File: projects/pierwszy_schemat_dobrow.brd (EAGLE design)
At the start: 100 x 80 mm, 37 parts, among them IC1 74HC595N, IC2 7805T, IC3 LD117AV, J1 DCJ0202

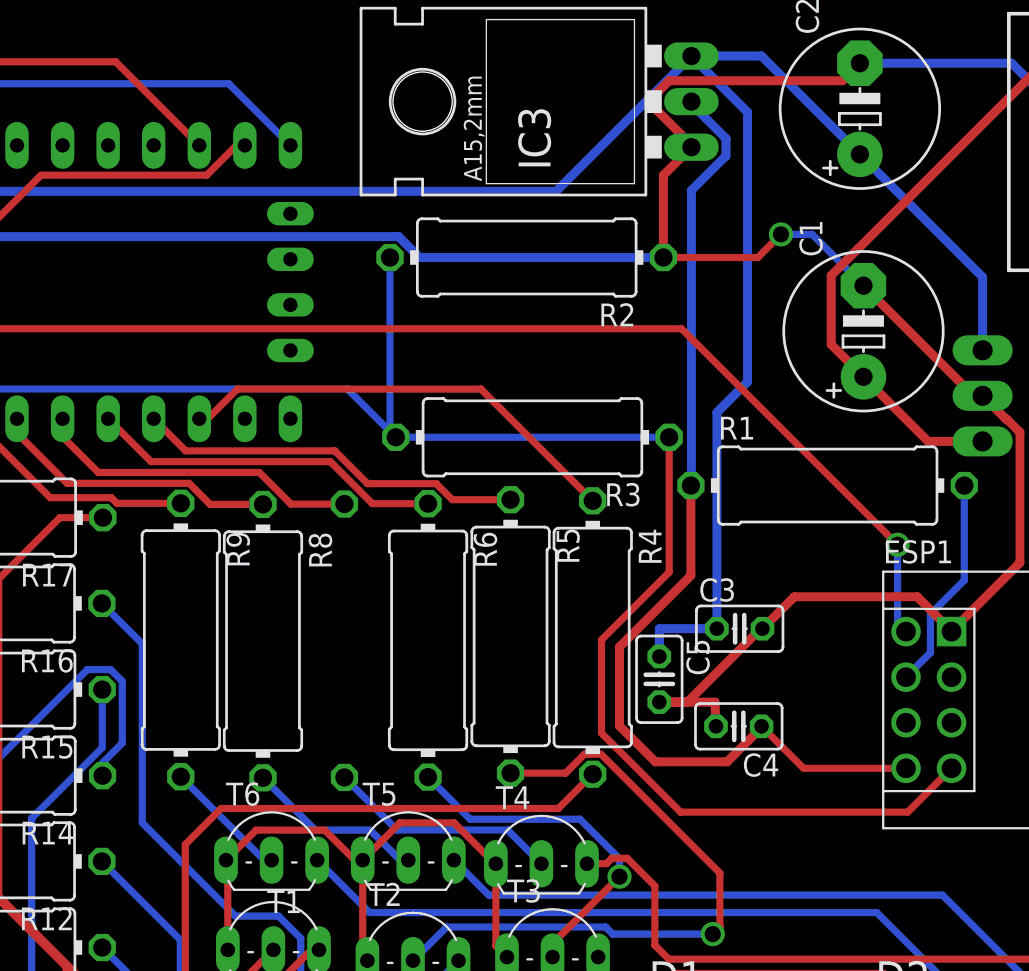
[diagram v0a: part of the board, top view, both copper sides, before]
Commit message: moved resistors for better thermal flow
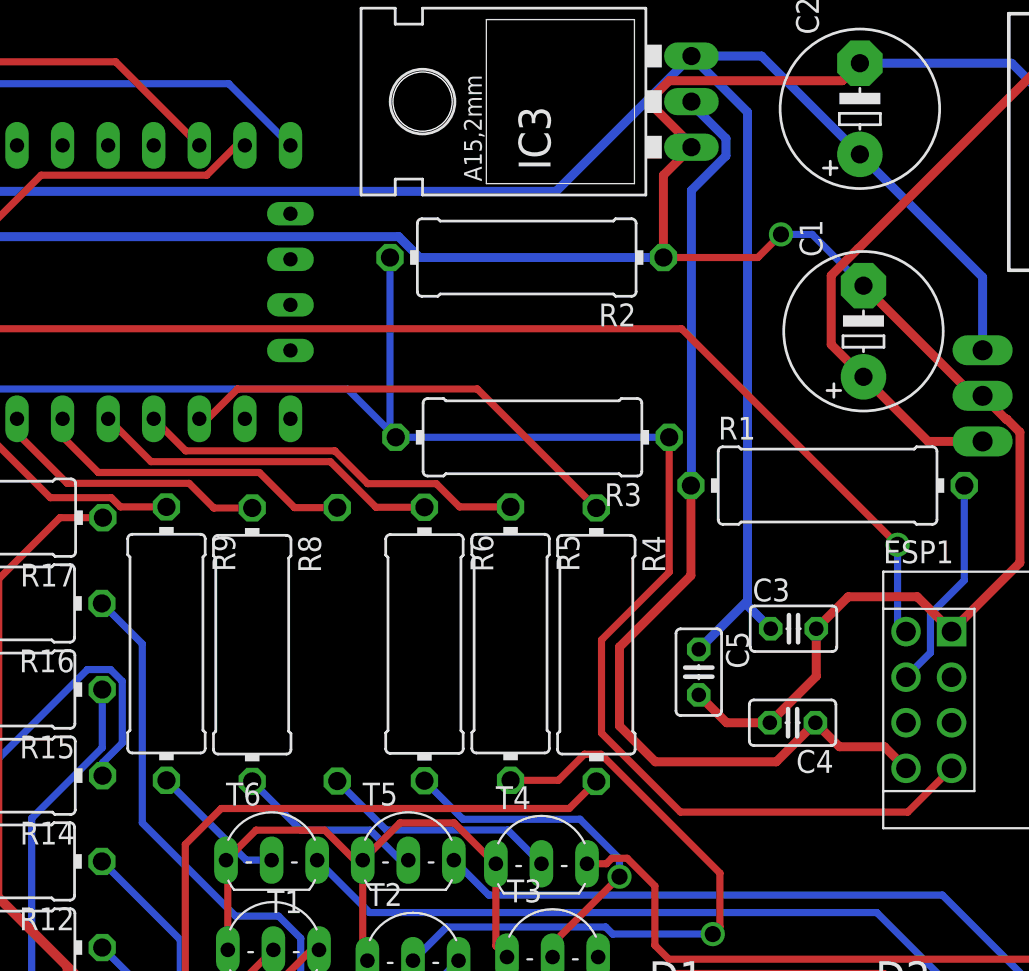
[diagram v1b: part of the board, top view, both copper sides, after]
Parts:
- moved C4 3.01 mm to (69.0, 39.0)
- moved C3 3.00 mm to (69.1, 44.2)
- moved C5 2.24 mm to (63.8, 41.8)
- moved R9 0.82 mm to (34.1, 43.4)
- moved R8 0.63 mm to (38.9, 43.3)
- moved R4 0.45 mm to (58.1, 43.3)
- moved R7 0.45 mm to (43.7, 43.4)
- moved R5 0.40 mm to (53.3, 43.4)
- moved R6 0.28 mm to (48.5, 43.4)
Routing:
- net GND: track 217.5 -> 213.5 mm
- net VCC_5V: track 156.3 -> 154.9 mm
- net N$6: track 6.99 -> 7.70 mm
- net N$36: track 13.6 -> 12.9 mm
- net N$5: track 10.0 -> 10.5 mm
- net N$35: track 16.2 -> 15.6 mm

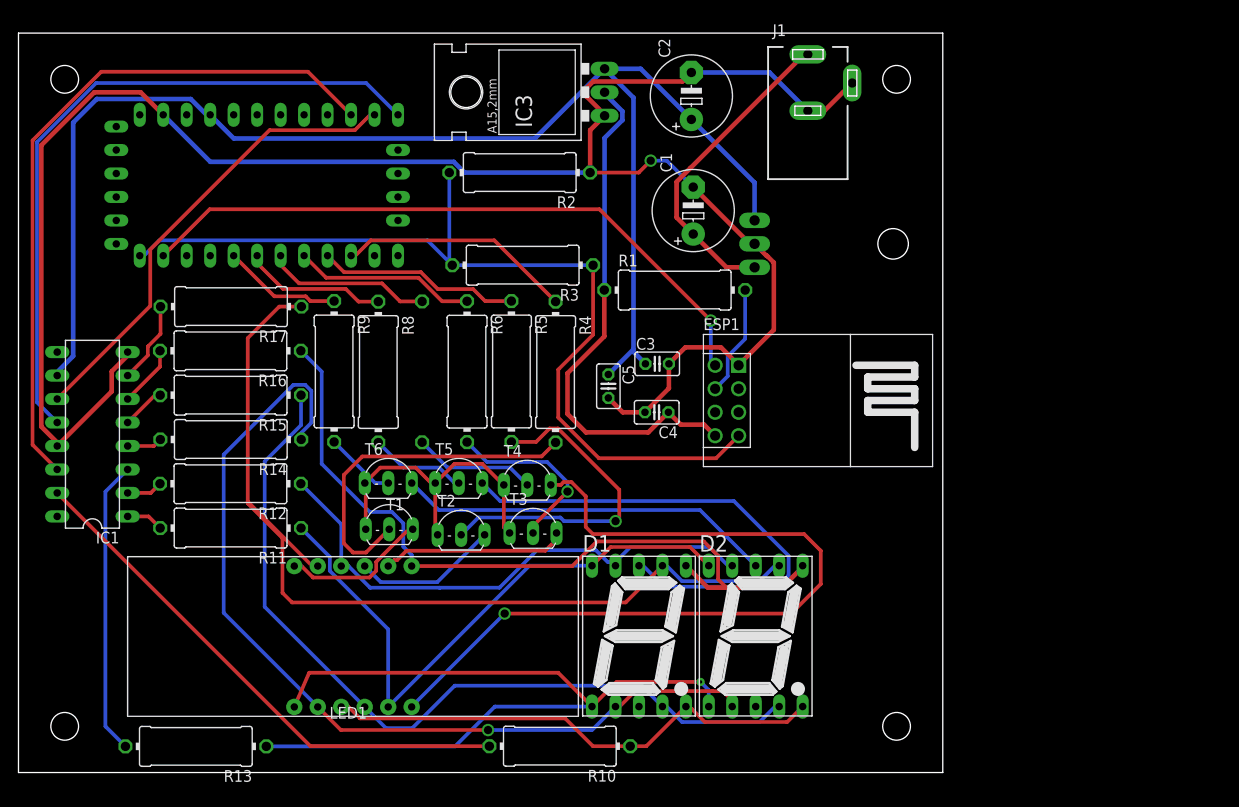
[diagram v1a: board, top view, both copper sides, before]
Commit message: Second revision of pcb layout
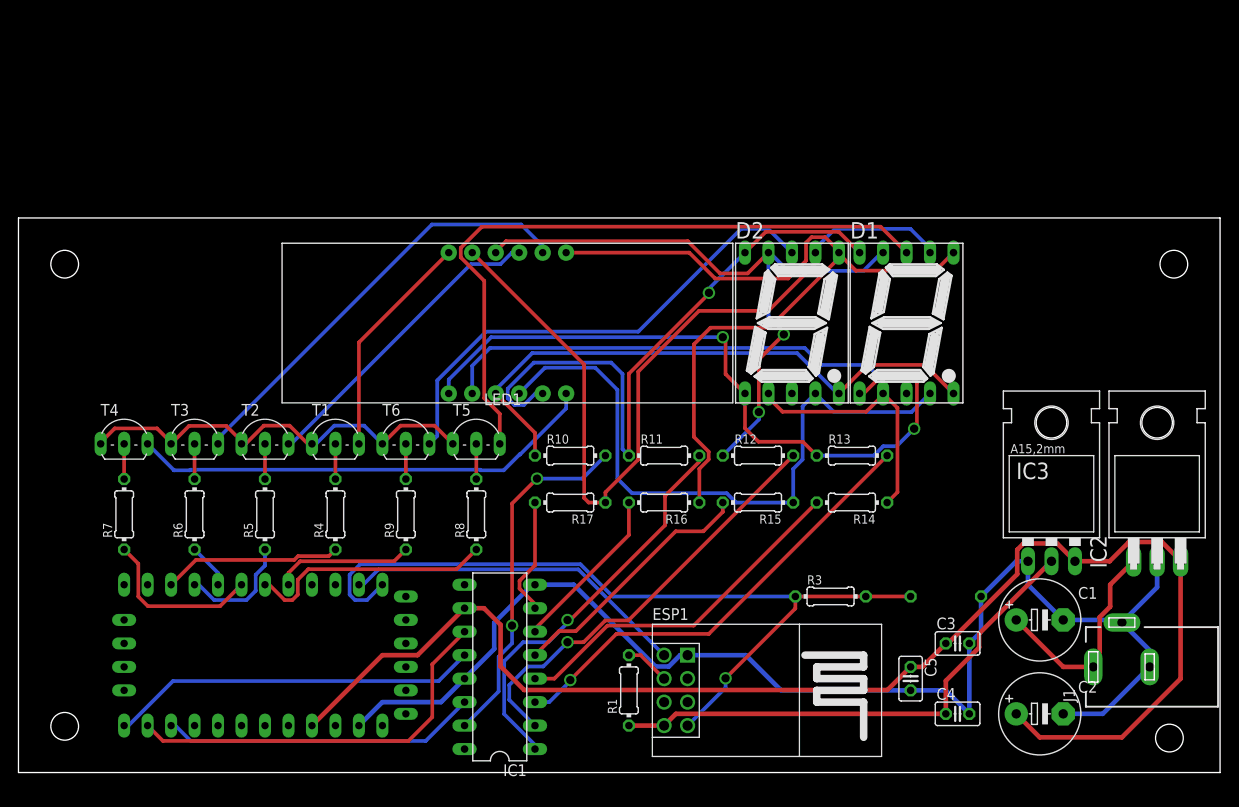
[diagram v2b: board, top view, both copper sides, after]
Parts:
- R1, R10, R11, R12, R13, R14, R15, R16, R17, R2, R3, R4, R5, R6, R7, R8, R9: device rcl:0414/15 -> rcl:0204/7
- moved R13 77.6 mm to (90.2, 34.3), turned to 0 degrees
- moved C2 76.7 mm to (110.5, 6.35), turned to 0 degrees
- moved J1 71.7 mm to (119.4, 11.4), turned to 90 degrees
- moved IC3 70.2 mm to (111.8, 26.7), turned to 0 degrees
- moved R14 67.5 mm to (90.2, 29.2)
- moved R2 65.0 mm to (100.3, 19.1), flipped to the bottom, turned to 0 degrees
- moved R15 58.2 mm to (80.0, 29.2)
- moved C1 58.0 mm to (110.5, 16.5), turned to 0 degrees
- moved R12 57.2 mm to (80.0, 34.3), turned to 0 degrees
- moved U$1 55.4 mm to (12.7, 14.0), turned to 270 degrees
- moved IC1 50.8 mm to (52.1, 11.4)
- moved R16 49.7 mm to (69.8, 29.2)
- moved R3 48.9 mm to (87.9, 19.1), turned to 0 degrees
- moved R11 47.6 mm to (69.8, 34.3), turned to 0 degrees
- moved C4 46.1 mm to (101.6, 6.35), turned to 0 degrees
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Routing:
- net GND: track 213.5 -> 140.8 mm, vias 1 -> 0
- net N$14: track 3.91 -> 46.5 mm, vias 0 -> 1
- net DATA_PIN: track 76.2 -> 34.2 mm
- net N$13: track 4.04 -> 43.6 mm, vias 0 -> 1
- net N$28: track 87.7 -> 51.0 mm, vias 1 -> 0
- net N$16: track 3.83 -> 38.4 mm
- net LATCH_PIN: track 74.4 -> 40.0 mm
- net N$1: track 38.1 -> 3.81 mm
- net RX_ARDUINO: track 71.3 -> 37.6 mm, vias 1 -> 0
- net N$2: track 36.2 -> 3.81 mm, vias 1 -> 0
- net N$27: track 20.1 -> 47.0 mm
- net N$17: track 4.75 -> 28.4 mm
- net SEG_C: track 89.9 -> 69.3 mm
- net SEG_D: track 98.8 -> 78.5 mm, vias 1 -> 0
- net N$12: track 58.1 -> 38.4 mm, vias 0 -> 2
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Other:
- board size 100 x 80 mm -> 130 x 60 mm
